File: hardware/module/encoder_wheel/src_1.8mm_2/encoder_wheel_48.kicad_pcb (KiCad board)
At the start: 2 copper layers, 74 x 74 mm, 2 parts

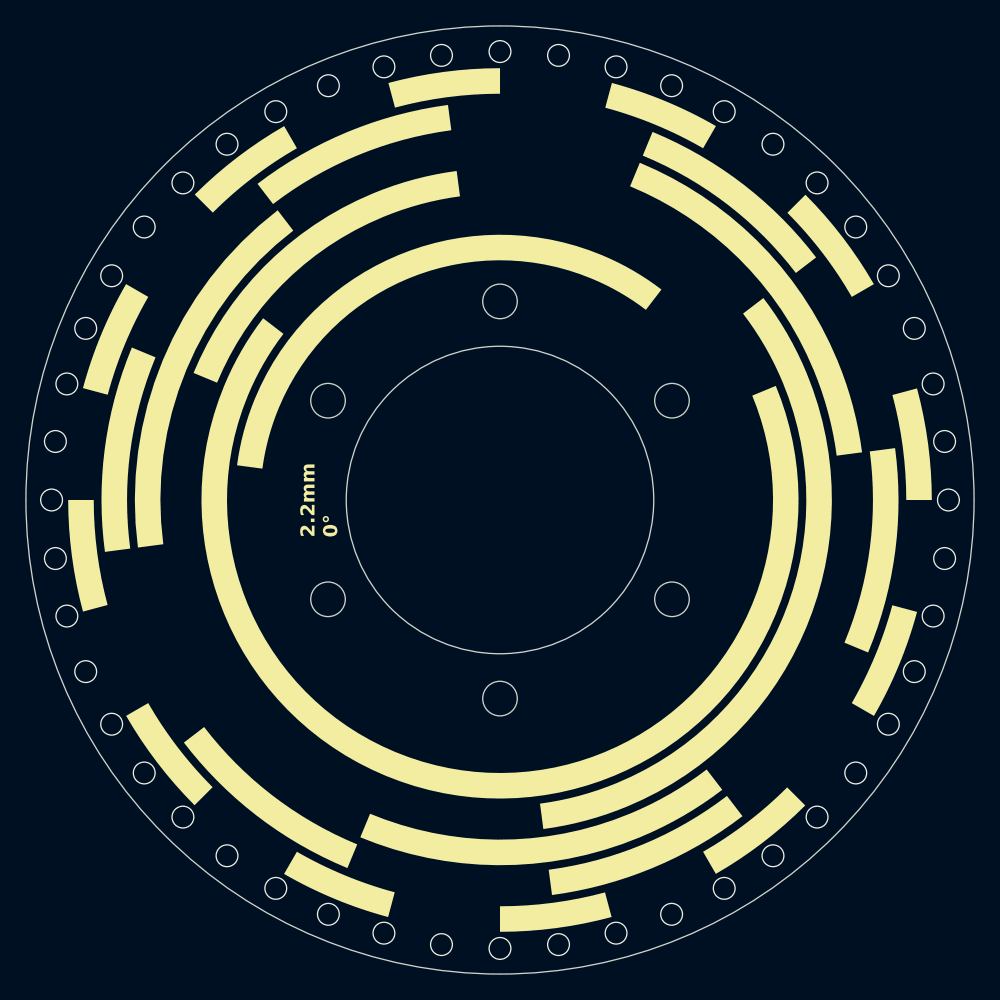
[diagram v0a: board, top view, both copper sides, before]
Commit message: add encoder wheel variants
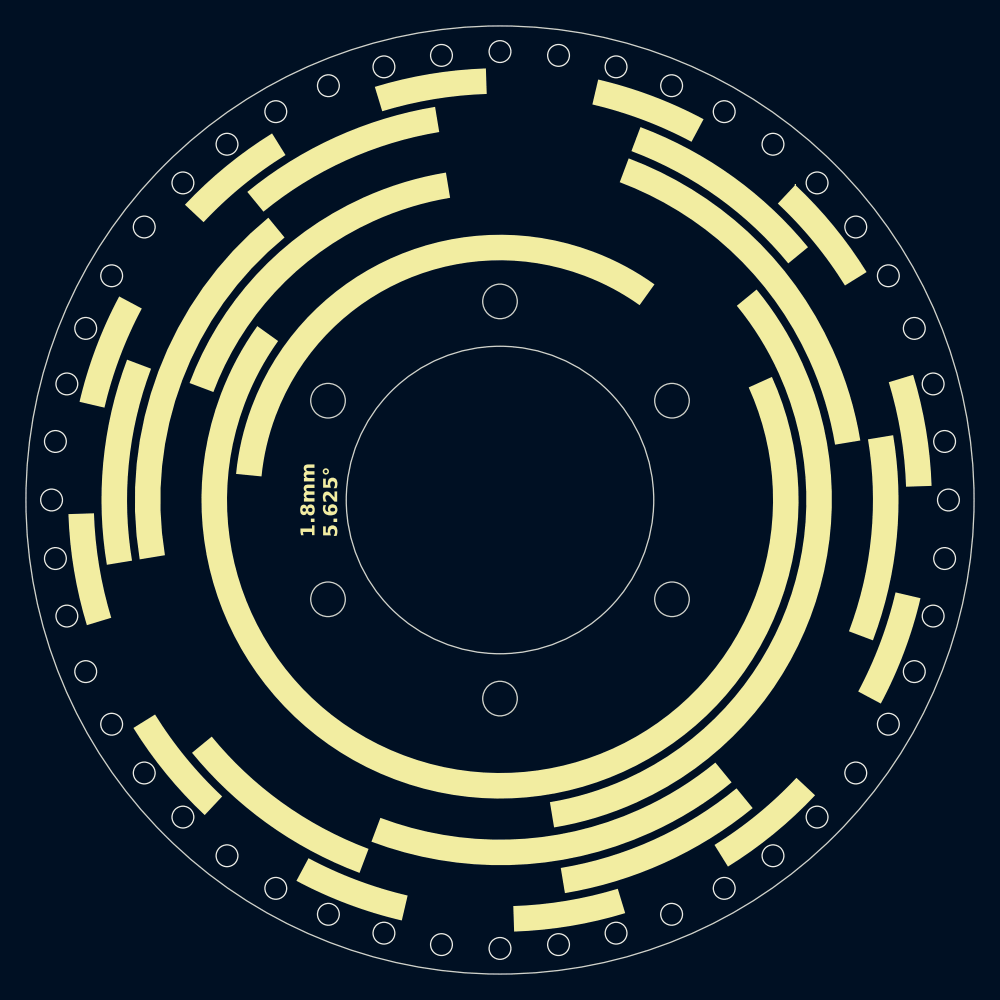
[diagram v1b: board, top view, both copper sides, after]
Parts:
- REF** (x2): value OpenFlapEncoderPattern48_2.2mm -> OpenFlapEncoderPattern48_1.8mm; footprint EncoderPattern:OpenFlapEncoderPattern48_2.2mm -> EncoderPattern:OpenFlapEncoderPattern48_1.8mm
- turned REF** to 1.875 degrees
- turned REF** to -178.125 degrees
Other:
- board text added: "1.8mm 1.875°"
- board text added: "1.8mm 5.625°"
- board text removed: "2.2mm 0°"
- board text removed: "2.2mm 3.75°"

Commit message: encoder changes
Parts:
- renumbered REF** to ENC1, REF** to ENC2

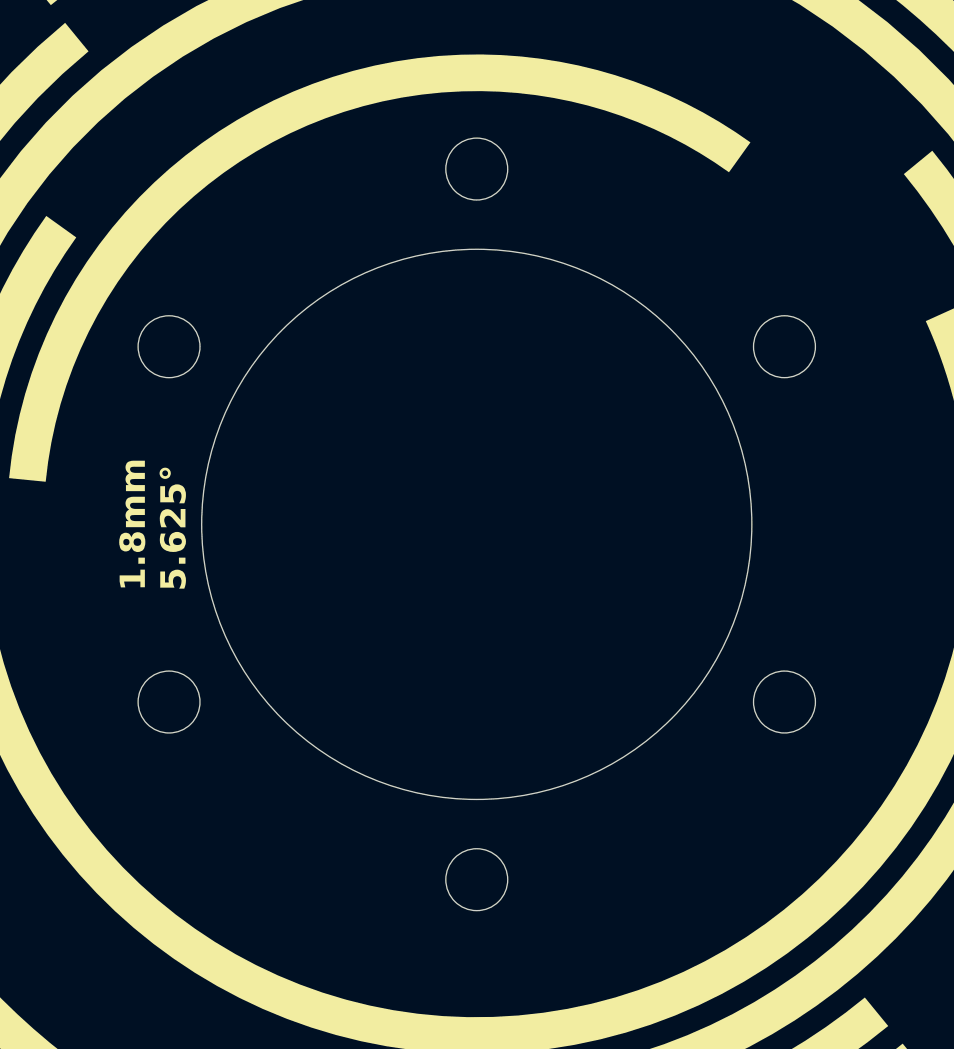
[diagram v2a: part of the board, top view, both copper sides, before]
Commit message: changed hole patern encoder wheel
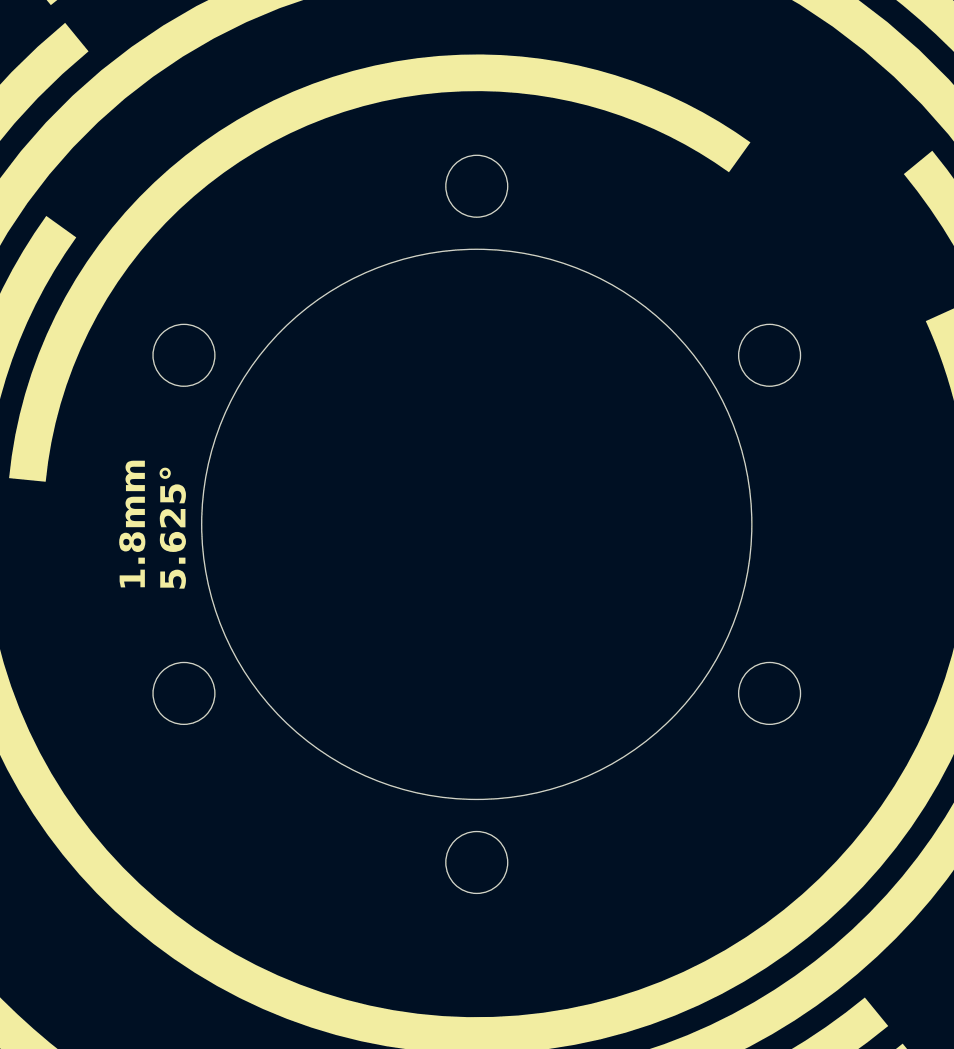
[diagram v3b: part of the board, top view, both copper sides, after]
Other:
- outline, holes or cut-outs redrawn
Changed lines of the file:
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@@
 				(xy -21.028138 -23.98439) (xy -21.416524 -23.63805) (xy -21.79918 -23.285501) (xy -22.176027 -22.92682)
 				(xy -22.546983 -22.562082) (xy -23.682314 -23.69793) (xy -22.89688 -24.457753) (xy -22.087029 -25.191793)
-				(xy -21.253427 -25.899402) (xy -20.396742 -26.579947) (xy -19.51764 -27.232774) (xy -18.616789 -27.857244)
+				(xy -21.253427 -25.8994) (xy -20.396742 -26.579947) (xy -19.51764 -27.232774) (xy -18.616789 -27.857244)
 				(xy -17.694855 -28.452712) (xy -16.752505 -29.018535)
 			)
@@
 				(xy -17.090735 23.796679) (xy -16.304792 24.343111) (xy -15.500463 24.864257) (xy -14.678322 25.359541)
 				(xy -13.838943 25.828387) (xy -12.982901 26.270221) (xy -12.110771 26.684465) (xy -11.223127 27.070544)
-				(xy -11.837043 28.552111) (xy -12.773694 28.145174) (xy -13.693925 27.70851) (xy -14.597137 27.242726)
+				(xy -11.837043 28.552111) (xy -12.773694 28.145174) (xy -13.693925 27.70851) (xy -14.597139 27.242726)
 				(xy -15.482717 26.748428) (xy -16.350072 26.226223) (xy -17.198594 25.676718) (xy -18.02768 25.10052)
 				(xy -18.836728 24.498237) (xy -19.625135 23.870473) (xy -20.392296 23.217837) (xy -21.137609 22.540936)
@@
 				(xy -12.833772 -28.117497) (xy -11.912166 -28.520661) (xy -10.975189 -28.894425) (xy -10.023417 -29.238206)
 				(xy -9.057427 -29.551421) (xy -8.077797 -29.833486) (xy -7.085104 -30.083819) (xy -6.079926 -30.301836)
-				(xy -5.062838 -30.486952) (xy -4.034419 -30.638591)
+				(xy -5.062838 -30.48695) (xy -4.034419 -30.638591)
 			)
 			(stroke
@@
 				(xy -25.972198 -11.2622) (xy -25.289807 -12.718712) (xy -24.528525 -14.128612) (xy -23.691203 -15.489057)
 				(xy -22.78069 -16.797208) (xy -21.799835 -18.050221) (xy -20.751489 -19.245257) (xy -19.6385 -20.379472)
-				(xy -18.463722 -21.450027) (xy -17.229995 -22.454078)
+				(xy -18.463724 -21.450027) (xy -17.229995 -22.454078)
 			)
 			(stroke
@@
 			(pts
 				(xy -17.052745 -13.083074) (xy -17.561869 -12.392777) (xy -18.04383 -11.681929) (xy -18.497845 -10.951294)
-				(xy -18.923129 -10.201633) (xy -19.318898 -9.433721) (xy -19.684367 -8.648311) (xy -20.018752 -7.846172)
+				(xy -18.923129 -10.201631) (xy -19.318898 -9.433721) (xy -19.684367 -8.648311) (xy -20.018752 -7.846172)
 				(xy -20.321269 -7.028066) (xy -20.591133 -6.194759) (xy -20.827559 -5.347014) (xy -21.029765 -4.485597)
 				(xy -21.196964 -3.61127) (xy -21.328374 -2.724798) (xy -21.423209 -1.826945) (xy -21.480685 -0.918476)
@@
 				(xy 18.385937 11.145737) (xy 18.903815 10.245388) (xy 19.378798 9.318394) (xy 19.809532 8.366109)
 				(xy 20.194662 7.389887) (xy 20.532836 6.391082) (xy 20.822697 5.371049) (xy 21.062894 4.331141)
-				(xy 21.25207 3.272715) (xy 21.388873 2.197118) (xy 21.471947 1.105711) (xy 21.49994 -0.000154) (xy 21.493163 -0.544487)
+				(xy 21.25207 3.272717) (xy 21.388873 2.197118) (xy 21.471947 1.105711) (xy 21.49994 -0.000154) (xy 21.493163 -0.544487)
 				(xy 21.47294 -1.085486) (xy 21.439433 -1.622994) (xy 21.392806 -2.156853) (xy 21.333221 -2.686908)
 				(xy 21.26084 -3.212999) (xy 21.175826 -3.734971) (xy 21.078341 -4.252665) (xy 20.968548 -4.765924)
@@
 				(xy 32.362321 -8.683039) (xy 32.058363 -9.748326) (xy 31.720574 -10.798849) (xy 31.349549 -11.833965)
 				(xy 30.945887 -12.853031) (xy 30.510184 -13.855404) (xy 30.043036 -14.84044) (xy 29.54504 -15.807497)
-				(xy 29.016793 -16.75593) (xy 27.627213 -15.952879) (xy 28.13047 -15.049968) (xy 28.604936 -14.129371)
+				(xy 29.016793 -16.75593) (xy 27.627213 -15.952879) (xy 28.13047 -15.049968) (xy 28.604934 -14.129371)
 				(xy 29.050048 -13.191699) (xy 29.465224 -12.237563) (xy 29.849894 -11.267574) (xy 30.203484 -10.282341)
 				(xy 30.525421 -9.282477) (xy 30.815133 -8.268591)
@@
 				(xy -24.984767 -19.829953) (xy -24.657515 -20.234999) (xy -24.323825 -20.63456) (xy -23.983773 -21.028556)
 				(xy -23.637434 -21.416908) (xy -23.284883 -21.799537) (xy -22.926198 -22.176364) (xy -22.561452 -22.547308)
-				(xy -23.697817 -23.682639) (xy -24.457612 -22.897228) (xy -25.191642 -22.087376) (xy -25.899258 -21.253761)
+				(xy -23.697817 -23.682639) (xy -24.457612 -22.897228) (xy -25.191642 -22.087376) (xy -25.899258 -21.253763)
 				(xy -26.579811 -20.39705) (xy -27.232652 -19.517927) (xy -27.857134 -18.617065) (xy -28.452607 -17.695141)
 				(xy -29.018422 -16.752829) (xy -27.62781 -15.950812)
@@
 				(xy 6.716876 -28.525201) (xy 7.657807 -28.287629) (xy 8.586402 -28.019963) (xy 9.502109 -27.722755)
 				(xy 10.40438 -27.396559) (xy 11.292663 -27.041926) (xy 12.166409 -26.659411) (xy 13.025068 -26.249566)
-				(xy 13.868088 -25.812943) (xy 14.69492 -25.350096) (xy 15.505014 -24.861578) (xy 16.297819 -24.347938)
+				(xy 13.868088 -25.812943) (xy 14.69492 -25.350096) (xy 15.505014 -24.861578) (xy 16.297819 -24.347936)
 				(xy 17.072785 -23.809738) (xy 17.829362 -23.247523)
 			)
@@
 				(xy -18.836728 -24.498237) (xy -19.625135 -23.870473) (xy -20.392296 -23.217837) (xy -21.137609 -22.540936)
 				(xy -21.860471 -21.840376) (xy -22.560278 -21.116764) (xy -23.236427 -20.370707) (xy -23.888314 -19.602811)
-				(xy -24.515338 -18.813685) (xy -23.24203 -17.835963)
+				(xy -24.515338 -18.813685) (xy -23.24203 -17.835961)
 			)
 			(stroke
@@
 			(pts
 				(xy -16.25176 21.178704) (xy -17.415705 20.231117) (xy -18.524109 19.220839) (xy -19.574276 18.150561)
-				(xy -20.563506 17.02297) (xy -21.489098 15.840755) (xy -22.348365 14.606605) (xy -23.138598 13.323208)
+				(xy -20.563506 17.02297) (xy -21.489096 15.840755) (xy -22.348365 14.606605) (xy -23.138598 13.323208)
 				(xy -23.857104 11.993253) (xy -24.501183 10.619428) (xy -25.068138 9.204422) (xy -25.555272 7.750925)
 				(xy -25.959886 6.261623) (xy -26.279282 4.739207) (xy -26.510762 3.186364) (xy -26.651628 1.605784)
@@
 				(xy -0.000041 -28.300959) (xy -0.71743 -28.292034) (xy -1.430394 -28.265403) (xy -2.138727 -28.221281)
 				(xy -2.842221 -28.159883) (xy -3.540671 -28.081424) (xy -4.233868 -27.986118) (xy -4.921605 -27.874181)
-				(xy -5.603677 -27.745827) (xy -6.279875 -27.601272) (xy -6.949993 -27.440728) (xy -7.613823 -27.264418)
+				(xy -5.603677 -27.745827) (xy -6.279875 -27.601272) (xy -6.949993 -27.440726) (xy -7.613823 -27.264418)
 				(xy -8.271159 -27.072548) (xy -8.921794 -26.865337) (xy -9.565521 -26.642999) (xy -10.202132 -26.40575)
 				(xy -10.83142 -26.153803) (xy -10.216987 -24.67121) (xy -9.623267 -24.909187) (xy -9.022652 -25.133286)
@@
 				(xy 10.893207 15.438515) (xy 10.268324 15.862183) (xy 9.626055 16.261283) (xy 8.96707 16.635126)
 				(xy 8.292042 16.983022) (xy 7.601642 17.304283) (xy 6.896542 17.598219) (xy 6.177413 17.864141)
-				(xy 5.444928 18.101359) (xy 4.699757 18.309184) (xy 3.942573 18.486925) (xy 3.174047 18.6339) (xy 2.394851 18.749411)
+				(xy 5.444928 18.101359) (xy 4.699757 18.309184) (xy 3.942573 18.486923) (xy 3.174047 18.6339) (xy 2.394851 18.749411)
 				(xy 1.605657 18.832773) (xy 0.807135 18.883295) (xy -0.000041 18.900289) (xy -0.894398 18.879458)
 				(xy -1.778065 18.817584) (xy -2.650117 18.715592) (xy -3.509631 18.574411) (xy -4.355682 18.394966)
@@
 				(xy -9.875451 17.97149) (xy -9.066096 18.393694) (xy -8.236062 18.780433) (xy -7.386347 19.130707)
 				(xy -6.517951 19.443516) (xy -5.631873 19.71786) (xy -4.729113 19.952741) (xy -3.810669 20.147157)
-				(xy -2.877541 20.300111) (xy -1.930727 20.410601) (xy -0.971227 20.477628) (xy -0.000038 20.500192)
+				(xy -2.877541 20.300111) (xy -1.930727 20.410601) (xy -0.971227 20.477628) (xy -0.000037 20.500192)
 			)
 			(stroke
@@
 	)
 	(gr_circle
-		(center 87.576606 107.75)
-		(end 88.926606 107.75)
+		(center 88.226125 107.375)
+		(end 89.576125 107.375)
 		(stroke
 			(width 0.05)
@@
 	)
 	(gr_circle
-		(center 101 84.5)
-		(end 102.35 84.5)
+		(center 101 85.25)
+		(end 102.35 85.25)
 		(stroke
 			(width 0.05)
@@
 	)
 	(gr_circle
-		(center 114.423394 92.25)
-		(end 115.773394 92.25)
+		(center 113.773875 92.625)
+		(end 115.123875 92.625)
 		(stroke
 			(width 0.05)
@@
 	)
 	(gr_circle
-		(center 87.576606 92.25)
-		(end 88.926606 92.25)
+		(center 88.226125 92.625)
+		(end 89.576125 92.625)
 		(stroke
 			(width 0.05)
@@
 	)
 	(gr_circle
-		(center 114.423394 107.75)
-		(end 115.773394 107.75)
+		(center 113.773875 107.375)
+		(end 115.123875 107.375)
 		(stroke
 			(width 0.05)
@@
 	)
 	(gr_circle
-		(center 101 115.5)
-		(end 102.35 115.5)
+		(center 101 114.75)
+		(end 102.35 114.75)
 		(stroke
 			(width 0.05)
